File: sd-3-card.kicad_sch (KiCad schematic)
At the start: 20 parts

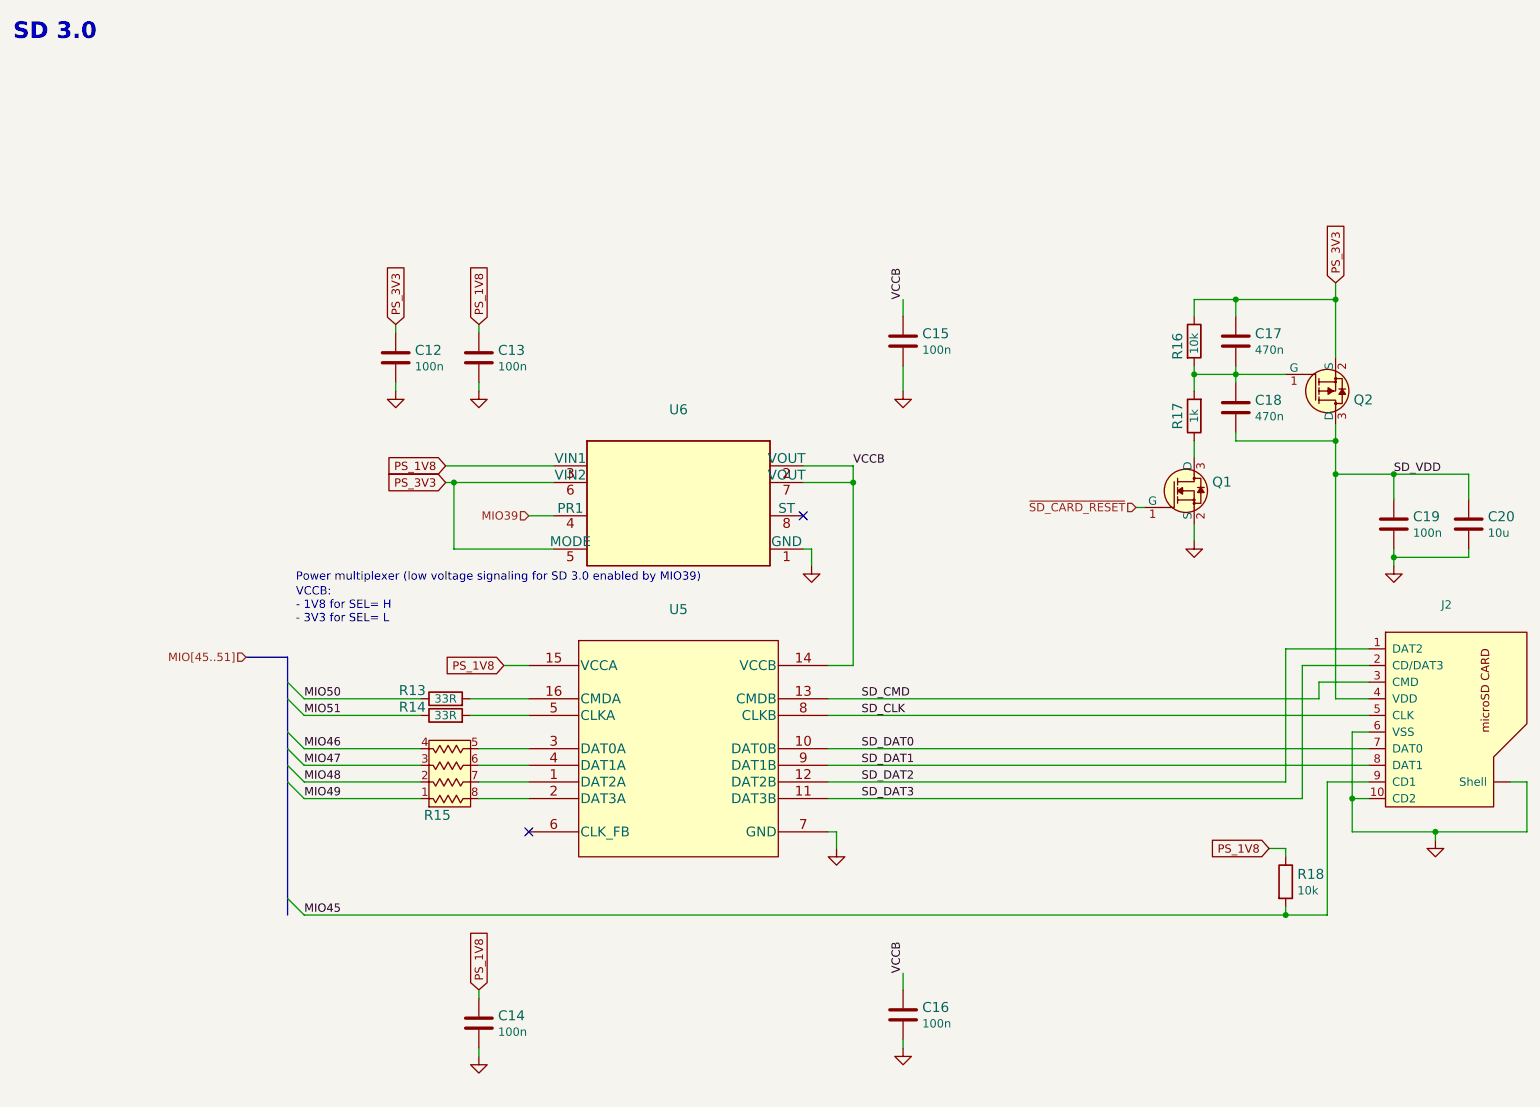
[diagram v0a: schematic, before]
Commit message: Fixed U45 direction issue
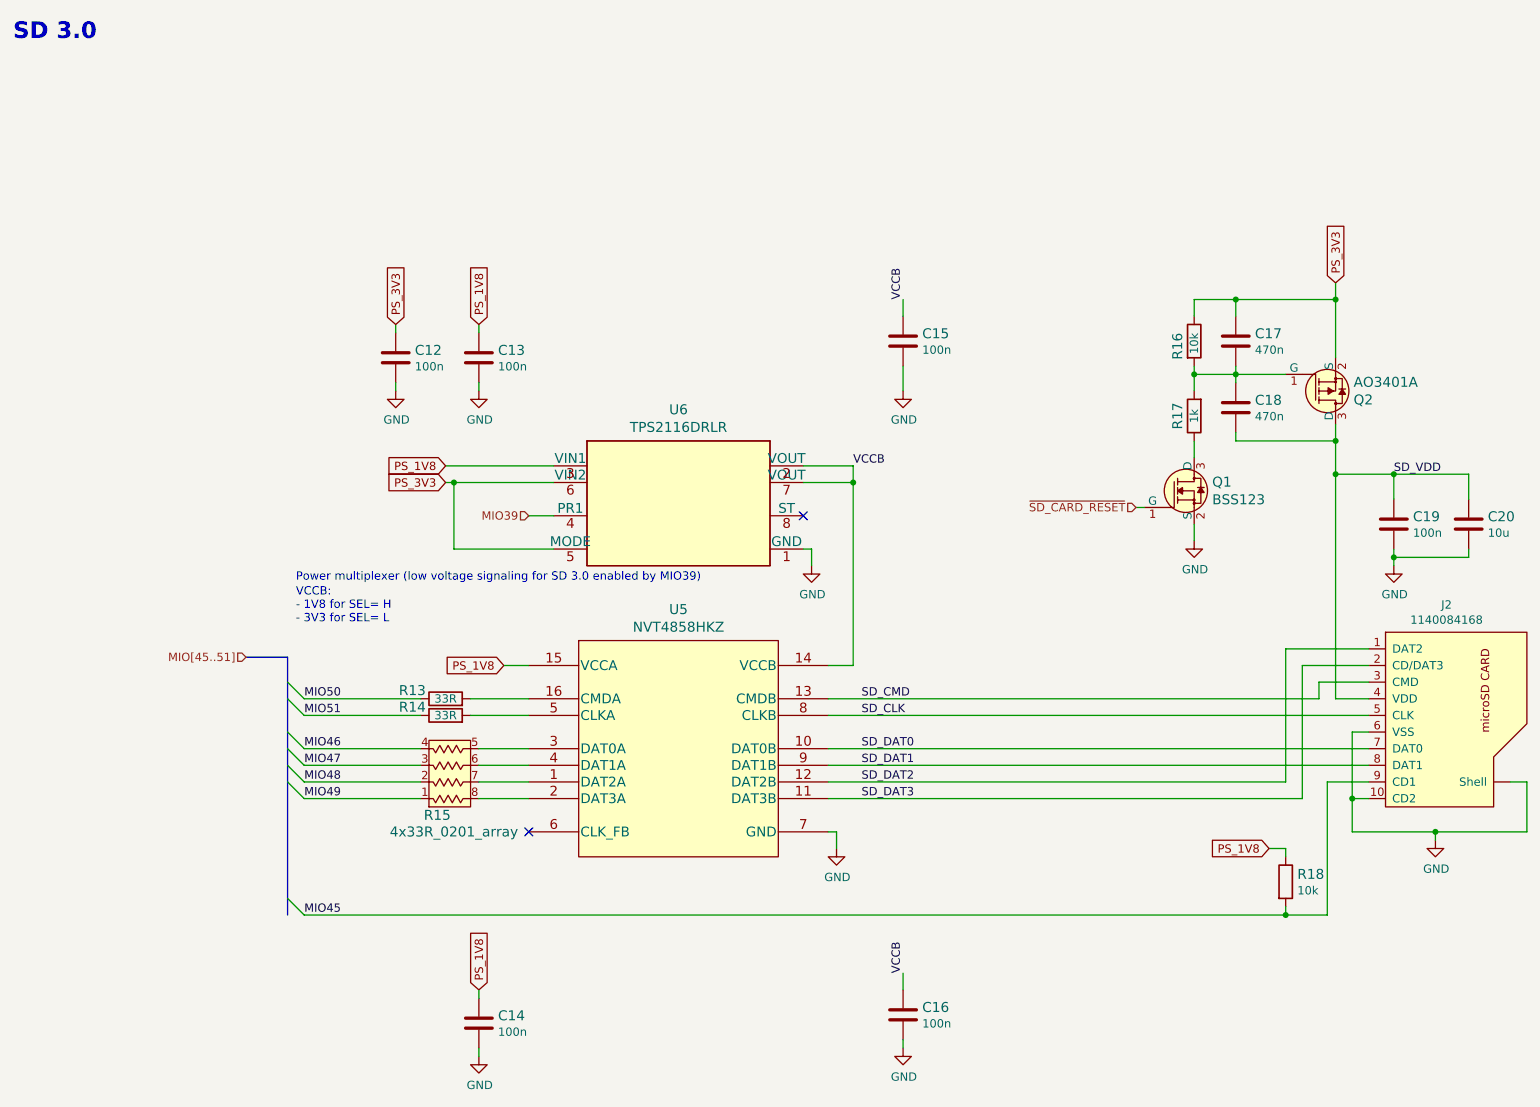
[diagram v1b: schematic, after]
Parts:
- C12, C13, C14, C15, C16, C19: value (none) -> C_100n_0402; footprint (none) -> kria-k26-devboard-footprints:0402-cap
- C17, C18: value (none) -> C_470n_0402; footprint (none) -> kria-k26-devboard-footprints:0402-cap
- C20: value (none) -> C_10u_0603; footprint (none) -> kria-k26-devboard-footprints:0603-cap
- J2: value (none) -> 1140084168; footprint (none) -> kria-k26-devboard-footprints:MicroSD_1140084168
- Q1: value (none) -> BSS123; footprint (none) -> kria-k26-devboard-footprints:SOT-23-3
- Q2: value (none) -> AO3401A; footprint (none) -> kria-k26-devboard-footprints:SOT-23-3
- R13, R14: value (none) -> R_33R_0402; footprint (none) -> kria-k26-devboard-footprints:0402-res
- R15: value (none) -> 4x33R_0201_array; footprint (none) -> kria-k26-devboard-footprints:EXB18V
- R16, R18: value (none) -> R_10k_0402; footprint (none) -> kria-k26-devboard-footprints:0402-res
- R17: value (none) -> R_1k_0402; footprint (none) -> kria-k26-devboard-footprints:0402-res
- U5: value (none) -> NVT4858HKZ; footprint (none) -> kria-k26-devboard-footprints:SOT1161-2
- U6: value (none) -> TPS2116DRLR; footprint (none) -> kria-k26-devboard-footprints:Texas_DRL0008A

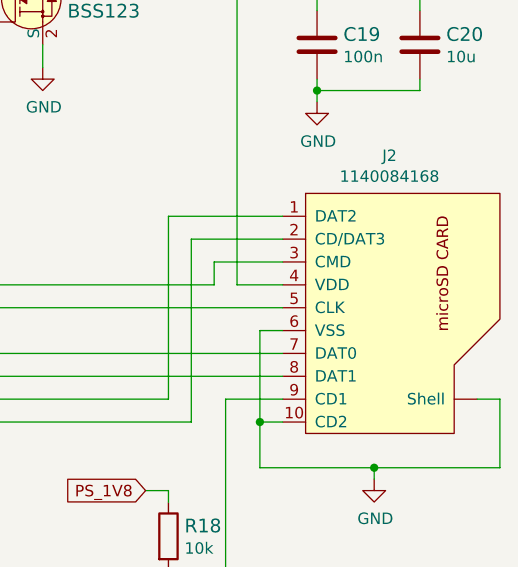
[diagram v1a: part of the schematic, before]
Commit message: Fixed 1140084168 lib causing errors, reconfigure and clear DRC after migration to KiCad 6
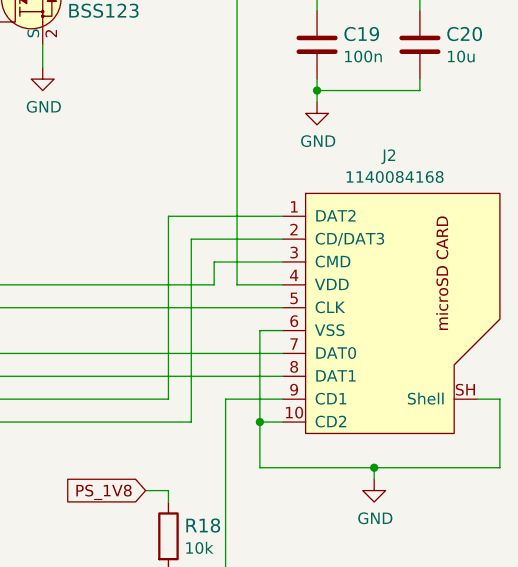
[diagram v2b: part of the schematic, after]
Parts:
- J2: footprint kria-k26-devboard-footprints:MicroSD_1140084168 -> antmicro-footprints:MicroSD_1140084168; symbol kria-k26-devboard:1140084168 -> antmicroMemoryConnectorsPCCardSockets:1140084168
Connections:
- net GND: now also J2.SH (Shell); no longer J2.~ (Shell)
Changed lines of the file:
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@@
     (pin "9")
   )
-  (symbol (lib_id "kria-k26-devboard:1140084168") (at 234.95 123.19 0) (unit 1)
+  (symbol (lib_id "antmicroMemoryConnectorsPCCardSockets:1140084168") (at 234.95 123.19 0) (unit 1)
     (in_bom yes) (on_board yes)
     (property "Reference" "J2" (id 0) (at 234.1118 105.029 0))
-    (property "Value" "1140084168" (id 1) (at 234.1118 107.3404 0))
-    (property "Footprint" "kria-k26-devboard-footprints:MicroSD_1140084168" (id 2) (at 232.41 139.7 0)
+    (property "Value" "1140084168" (id 1) (at 234.696 107.442 0))
+    (property "Footprint" "antmicro-footprints:MicroSD_1140084168" (id 2) (at 232.41 139.7 0)
       (effects (font (size 1.27 1.27)) hide)
     )
@@
     (pin "8")
     (pin "9")
-    (pin "~")
+    (pin "SH")
   )
   (symbol (lib_id "kria-k26-devboard:TPS2116DRLR") (at 97.79 83.82 0) (unit 1)

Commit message: Loclib of project in KiCad 6 format. Removed old KiCad 5 files
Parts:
- J2: footprint antmicro-footprints:MicroSD_1140084168 -> kria-k26-devboard-footprints:MicroSD_1140084168; symbol antmicroMemoryConnectorsPCCardSockets:1140084168 -> kria-k26-devboard:1140084168
